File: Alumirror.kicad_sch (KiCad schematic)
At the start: 42 parts, among them J1 USB_C_Receptacle_USB2.0_16P_2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, J2 USB_C_Receptacle_USB2.0_16P_2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, J3 USB_C_Receptacle_USB2.0_16P_2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, J4 USB_C_Receptacle_USB2.0_16P_2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, SW10 BOOT, U1 CH552T, U2 CH552T, U3 USBLC6-2P6, U4 USBLC6-2P6, U5 USBLC6-2P6, U6 USBLC6-2P6

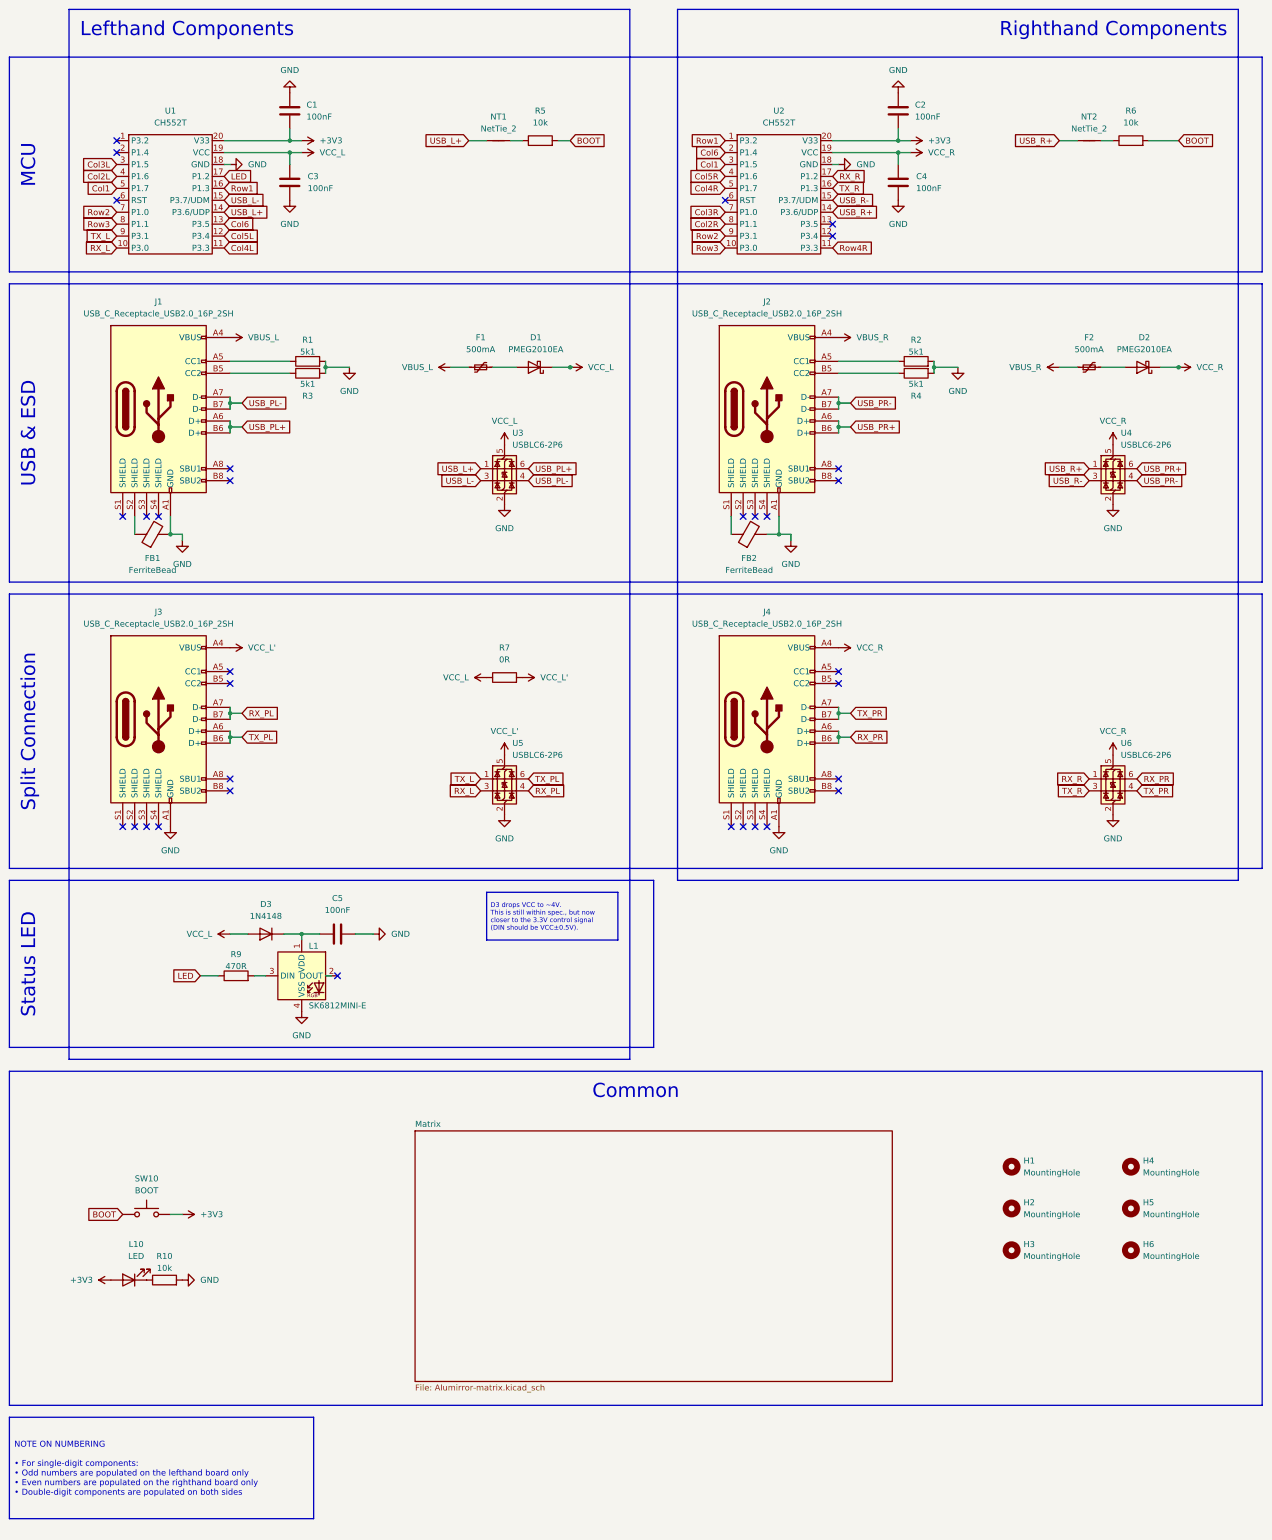
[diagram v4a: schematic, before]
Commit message: Update resistor values
Testing seemed to show that 5.1KΩ will work well for a dim power LED.
The value for the boot resistor is not well defined, but values from 5.1KΩ to 20KΩ have been seem.
(Using 5.1KΩ for these means that the same resistor stock used for USB power control can be used.)
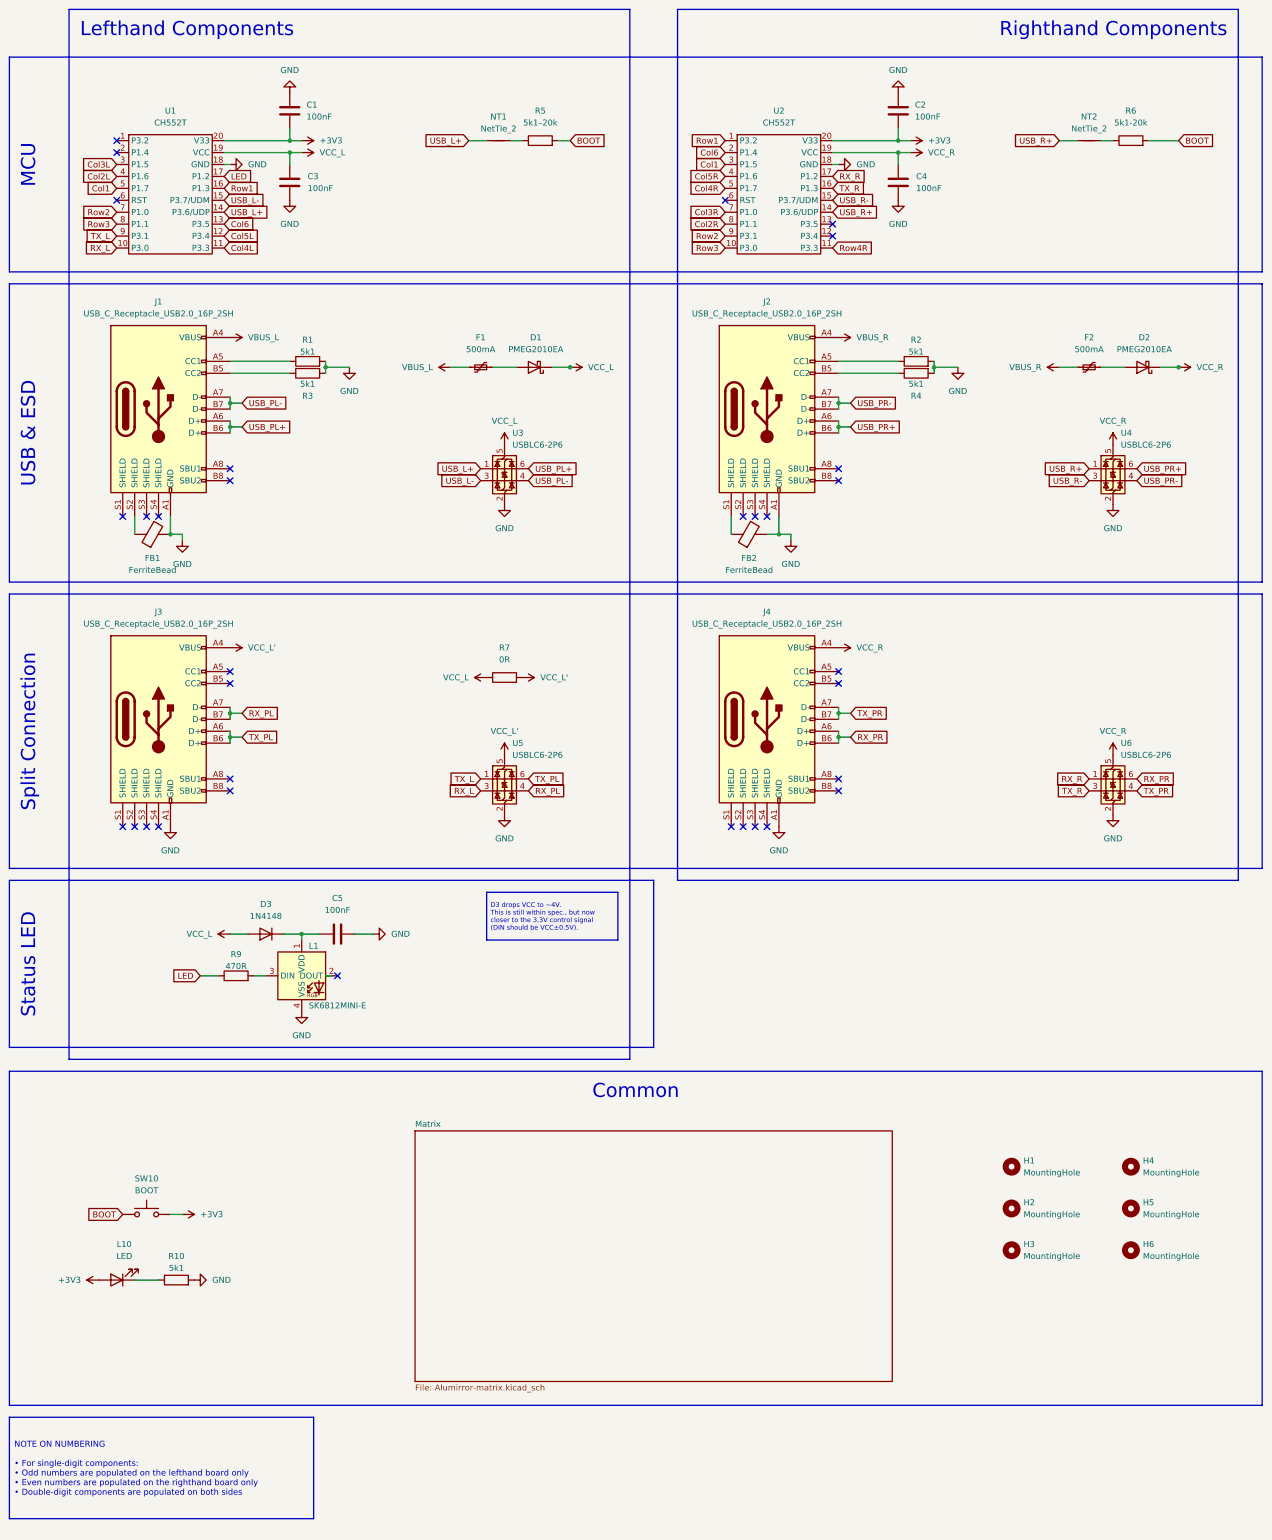
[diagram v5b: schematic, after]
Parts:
- R10: value 10k -> 5k1
- R5: value 10k -> 5k1–20k
- R6: value 10k -> 5k1-20k
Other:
- moved on the sheet: L10, R10
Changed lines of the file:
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@@
 	(wire
 		(pts
+			(xy 41.91 285.75) (xy 46.99 285.75)
+		)
+		(stroke
+			(width 0)
+			(type default)
+		)
+	)
+	(wire
+		(pts
 			(xy 62.23 102.87) (xy 62.23 104.14)
 		)
@@
 	(symbol
 		(lib_id "Device:LED")
-		(at 40.64 285.75 180)
+		(at 38.1 285.75 180)
 		(unit 1)
 		(exclude_from_sim no)
@@
 		(fields_autoplaced yes)
 		(property "Reference" "L10"
-			(at 42.2275 278.13 0)
+			(at 39.6875 278.13 0)
 			(effects
 				(font
@@
 		)
 		(property "Value" "LED"
-			(at 42.2275 280.67 0)
+			(at 39.6875 280.67 0)
 			(effects
 				(font
@@
 		)
 		(property "Footprint" "Project Library:LED_0805_2012Metric_Mod"
-			(at 40.64 285.75 0)
+			(at 38.1 285.75 0)
 			(effects
 				(font
@@
 		)
 		(property "Datasheet" "~"
-			(at 40.64 285.75 0)
+			(at 38.1 285.75 0)
 			(effects
 				(font
@@
 		)
 		(property "Description" "Light emitting diode"
-			(at 40.64 285.75 0)
+			(at 38.1 285.75 0)
 			(effects
 				(font
@@
 			)
 		)
-		(property "Value" "10k"
+		(property "Value" "5k1–20k"
 			(at 128.27 39.37 90)
 			(effects
@@
 	(symbol
 		(lib_id "power:VCC")
-		(at 36.83 285.75 90)
+		(at 34.29 285.75 90)
 		(unit 1)
 		(exclude_from_sim no)
@@
 		(fields_autoplaced yes)
 		(property "Reference" "#PWR020"
-			(at 40.64 285.75 0)
+			(at 38.1 285.75 0)
 			(effects
 				(font
@@
 		)
 		(property "Value" "+3V3"
-			(at 33.02 285.7499 90)
+			(at 30.48 285.7499 90)
 			(effects
 				(font
@@
 		)
 		(property "Footprint" ""
-			(at 36.83 285.75 0)
+			(at 34.29 285.75 0)
 			(effects
 				(font
@@
 		)
 		(property "Datasheet" ""
-			(at 36.83 285.75 0)
+			(at 34.29 285.75 0)
 			(effects
 				(font
@@
 		)
 		(property "Description" ""
-			(at 36.83 285.75 0)
+			(at 34.29 285.75 0)
 			(effects
 				(font
@@
 	(symbol
 		(lib_id "power:GND")
-		(at 52.07 285.75 90)
+		(at 54.61 285.75 90)
 		(unit 1)
 		(exclude_from_sim no)
@@
 		(fields_autoplaced yes)
 		(property "Reference" "#PWR021"
-			(at 58.42 285.75 0)
+			(at 60.96 285.75 0)
 			(effects
 				(font
@@
 		)
 		(property "Value" "GND"
-			(at 55.88 285.7499 90)
+			(at 58.42 285.7499 90)
 			(effects
 				(font
@@
 		)
 		(property "Footprint" ""
-			(at 52.07 285.75 0)
+			(at 54.61 285.75 0)
 			(effects
 				(font
@@
 		)
 		(property "Datasheet" ""
-			(at 52.07 285.75 0)
+			(at 54.61 285.75 0)
 			(effects
 				(font
@@
 		)
 		(property "Description" "Power symbol creates a global label with name \"GND\" , ground"
-			(at 52.07 285.75 0)
+			(at 54.61 285.75 0)
 			(effects
 				(font
@@
 			)
 		)
-		(property "Value" "10k"
+		(property "Value" "5k1-20k"
 			(at 254 39.37 90)
 			(effects
@@
 	(symbol
 		(lib_id "Device:R")
-		(at 48.26 285.75 90)
+		(at 50.8 285.75 90)
 		(unit 1)
 		(exclude_from_sim no)
@@
 		(dnp no)
 		(property "Reference" "R10"
-			(at 48.26 280.67 90)
+			(at 50.8 280.67 90)
 			(effects
 				(font
@@
 			)
 		)
-		(property "Value" "10k"
-			(at 48.26 283.21 90)
+		(property "Value" "5k1"
+			(at 50.8 283.21 90)
 			(effects
 				(font
@@
 		)
 		(property "Footprint" "Resistor_SMD:R_0603_1608Metric"
-			(at 48.26 287.528 90)
+			(at 50.8 287.528 90)
 			(effects
 				(font
@@
 		)
 		(property "Datasheet" "~"
-			(at 48.26 285.75 0)
+			(at 50.8 285.75 0)
 			(effects
 				(font
@@
 		)
 		(property "Description" "Resistor"
-			(at 48.26 285.75 0)
+			(at 50.8 285.75 0)
 			(effects
 				(font

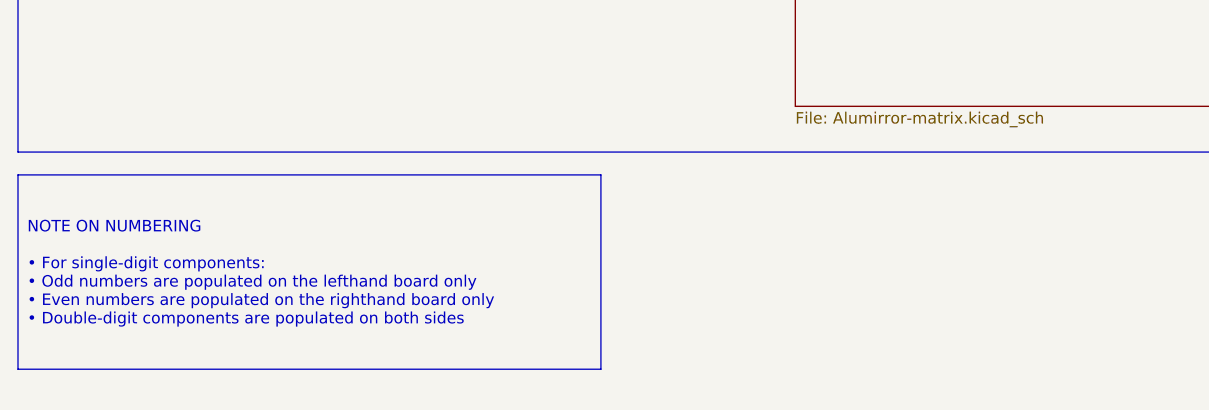
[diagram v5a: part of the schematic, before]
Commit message: Clean up cross-board column routing
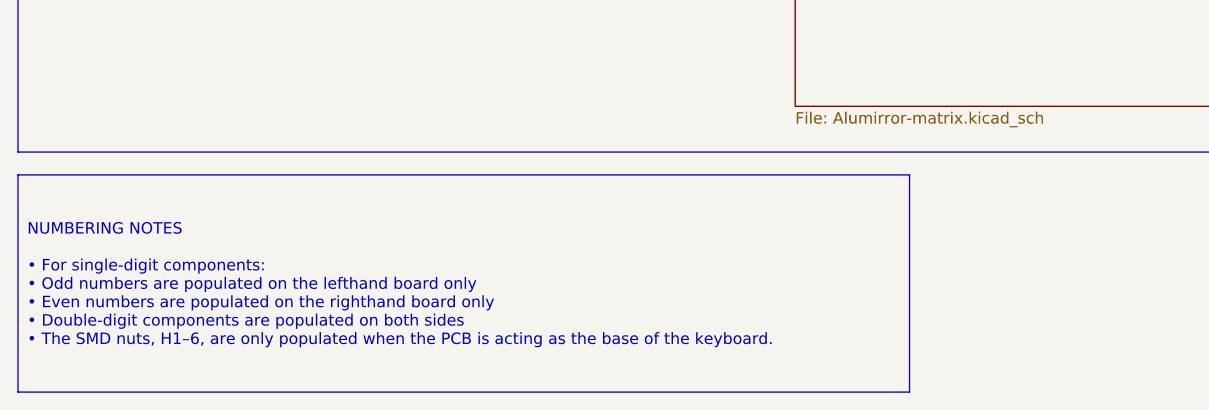
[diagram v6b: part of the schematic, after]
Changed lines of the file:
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@@
 		)
 	)
-	(text_box "NOTE ON NUMBERING\n\n• For single-digit components:\n  • Odd numbers are populated on the lefthand board only\n  • Even numbers are populated on the righthand board only\n• Double-digit components are populated on both sides"
+	(text_box "NUMBERING NOTES\n\n• For single-digit components:\n  • Odd numbers are populated on the lefthand board only\n  • Even numbers are populated on the righthand board only\n• Double-digit components are populated on both sides\n• The SMD nuts, H1–6, are only populated when the PCB is acting as the base of the keyboard."
 		(exclude_from_sim no)
 		(at 15.24 314.96 0)
-		(size 64.77 21.59)
+		(size 99.06 24.13)
 		(stroke
 			(width 0)
